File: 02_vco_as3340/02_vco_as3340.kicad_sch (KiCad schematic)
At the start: 98 parts, among them J10 SINE OUT, J3 SYNC IN, J4 FM IN, J5 PWM CV IN, J6 1V per O IN, J7 SQUARE OUT, J8 SAW OUT, J9 TRI OUT, Q1 BC847, Q2 BC847, SW2 SW_SPDT, U1 TL072, U2 AS3340, U3 TL074

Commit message: added diodes
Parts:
- removed SW1: (no value), cynthia:switch_linear_1x4, symbol cynthia:switch_linear_1x4
- added D3, D4: 1N5819WS, Diode_SMD:D_SOD-323, symbol Diode:1N5819WS
- added SW1: (no value), cynthia:switch_linear_2x4, symbol cynthia:switch_linear_2x4
- C7, C8: value 47uF -> 22uF
- SW2: footprint cynthia:switch -> cynthia:switch_spdt
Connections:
- net +12V: now also D4.1 (K); no longer H1.1 (Pin_1), H1.2 (Pin_2)
- net -12V: now also D3.2 (A); no longer H1.10 (Pin_10), H1.9 (Pin_9)
- net at C4.2: now also SW1.10, SW1.5
- net at C3.2: now also SW1.4, SW1.9
- net at C2.2: now also SW1.3, SW1.8
- net at J3.T: now also SW1.1, SW1.6
- net at C1.2: now also SW1.2, SW1.7
- new net: D4.2 (A), H1.1 (Pin_1), H1.2 (Pin_2)
- new net: D3.1 (K), H1.10 (Pin_10), H1.9 (Pin_9)

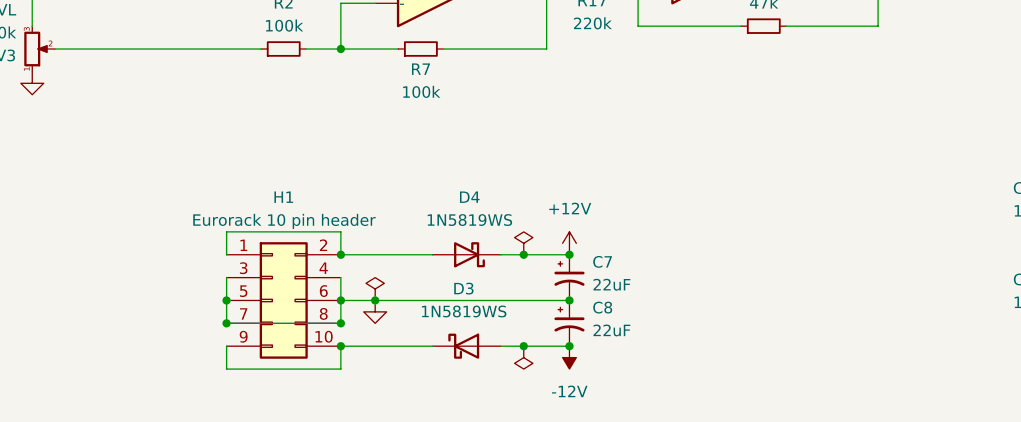
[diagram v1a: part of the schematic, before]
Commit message: added diodes to 02
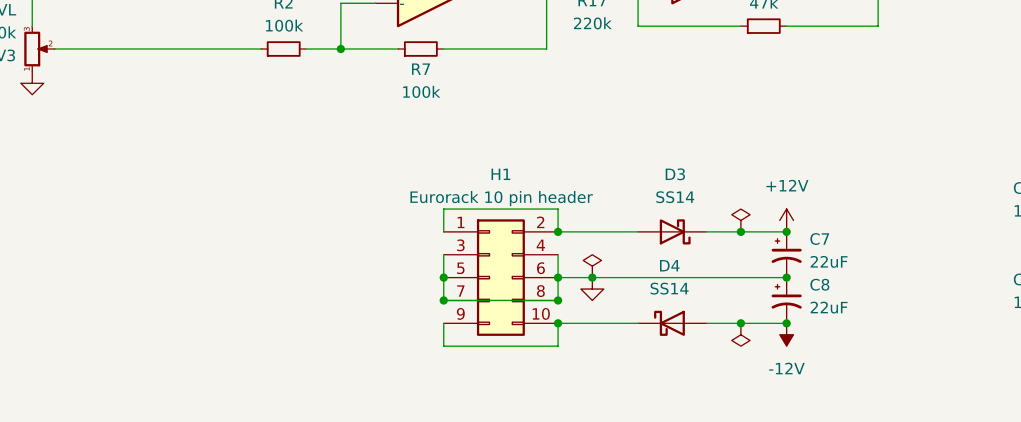
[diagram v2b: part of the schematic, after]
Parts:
- removed D3, D4: 1N5819WS, Diode_SMD:D_SOD-323, symbol Diode:1N5819WS
- added D3, D4: SS14, Diode_SMD:D_SMA, symbol Diode:SS14
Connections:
- net +12V: now also D3.1 (K)
- net -12V: now also D4.2 (A)
- net at H1.1 (Pin_1), H1.2 (Pin_2): now also D3.2 (A)
- net at H1.10 (Pin_10), H1.9 (Pin_9): now also D4.1 (K)
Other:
- moved on the sheet: C7, C8, H1

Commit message: cleaner PCB layout
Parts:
- D1, D2: footprint cynthia:C SMD 0805 -> Diode_SMD:D_SOD-323_HandSoldering
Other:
- moved on the sheet: RV1
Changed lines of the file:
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@@
 	(wire
 		(pts
-			(xy 107.95 222.25) (xy 111.76 222.25)
+			(xy 95.25 222.25) (xy 111.76 222.25)
 		)
 		(stroke
@@
 	(symbol
 		(lib_id "power:+12V")
-		(at 105.41 219.71 0)
+		(at 92.71 219.71 0)
 		(mirror y)
 		(unit 1)
@@
 		(fields_autoplaced yes)
 		(property "Reference" "#PWR054"
-			(at 105.41 223.52 0)
+			(at 92.71 223.52 0)
 			(hide yes)
 			(show_name no)
@@
 		)
 		(property "Value" "+12V"
-			(at 105.41 214.63 0)
+			(at 92.71 214.63 0)
 			(show_name no)
 			(do_not_autoplace no)
@@
 		)
 		(property "Footprint" ""
-			(at 105.41 219.71 0)
+			(at 92.71 219.71 0)
 			(hide yes)
 			(show_name no)
@@
 		)
 		(property "Datasheet" ""
-			(at 105.41 219.71 0)
+			(at 92.71 219.71 0)
 			(hide yes)
 			(show_name no)
@@
 		)
 		(property "Description" "Power symbol creates a global label with name \"+12V\""
-			(at 105.41 219.71 0)
+			(at 92.71 219.71 0)
 			(hide yes)
 			(show_name no)
@@
 	(symbol
 		(lib_id "Device:R_Potentiometer_Small")
-		(at 105.41 222.25 0)
+		(at 92.71 222.25 0)
 		(mirror x)
 		(unit 1)
@@
 		(dnp no)
 		(property "Reference" "RV1"
-			(at 103.886 224.536 0)
+			(at 91.186 224.536 0)
 			(show_name no)
 			(do_not_autoplace no)
@@
 		)
 		(property "Value" "250k"
-			(at 103.886 221.996 0)
+			(at 91.186 221.996 0)
 			(show_name no)
 			(do_not_autoplace no)
@@
 		)
 		(property "Footprint" "cynthia:potientiometer"
-			(at 105.41 222.25 0)
+			(at 92.71 222.25 0)
 			(hide yes)
 			(show_name no)
@@
 		)
 		(property "Datasheet" ""
-			(at 105.41 222.25 0)
+			(at 92.71 222.25 0)
 			(hide yes)
 			(show_name no)
@@
 		)
 		(property "Description" "PWM Offset"
-			(at 103.886 219.456 0)
+			(at 91.186 219.456 0)
 			(show_name no)
 			(do_not_autoplace no)
@@
 		)
 		(property "Sim.Device" "R"
-			(at 105.41 222.25 0)
+			(at 92.71 222.25 0)
 			(hide yes)
 			(show_name no)
@@
 		)
 		(property "Sim.Type" "POT"
-			(at 105.41 222.25 0)
+			(at 92.71 222.25 0)
 			(hide yes)
 			(show_name no)
@@
 		)
 		(property "Sim.Pins" "1=r0 2=wiper 3=r1"
-			(at 105.41 222.25 0)
+			(at 92.71 222.25 0)
 			(hide yes)
 			(show_name no)
@@
 			)
 		)
-		(property "Footprint" "cynthia:C SMD 0805"
+		(property "Footprint" "Diode_SMD:D_SOD-323_HandSoldering"
 			(at 128.27 151.13 90)
 			(hide yes)
@@
 	(symbol
 		(lib_id "power:-12V")
-		(at 105.41 224.79 180)
+		(at 92.71 224.79 180)
 		(unit 1)
 		(body_style 1)
@@
 		(fields_autoplaced yes)
 		(property "Reference" "#PWR04"
-			(at 105.41 227.33 0)
+			(at 92.71 227.33 0)
 			(hide yes)
 			(show_name no)
@@
 		)
 		(property "Value" "-12V"
-			(at 105.41 229.87 0)
+			(at 92.71 229.87 0)
 			(show_name no)
 			(do_not_autoplace no)
@@
 		)
 		(property "Footprint" ""
-			(at 105.41 224.79 0)
+			(at 92.71 224.79 0)
 			(hide yes)
 			(show_name no)
@@
 		)
 		(property "Datasheet" ""
-			(at 105.41 224.79 0)
+			(at 92.71 224.79 0)
 			(hide yes)
 			(show_name no)
@@
 		)
 		(property "Description" "Power symbol creates a global label with name \"-12V\""
-			(at 105.41 224.79 0)
+			(at 92.71 224.79 0)
 			(hide yes)
 			(show_name no)
@@
 			)
 		)
-		(property "Footprint" "cynthia:C SMD 0805"
+		(property "Footprint" "Diode_SMD:D_SOD-323_HandSoldering"
 			(at 128.27 158.75 90)
 			(hide yes)
